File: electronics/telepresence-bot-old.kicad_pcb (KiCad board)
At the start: 4 copper layers, 100 x 100 mm, 191 parts, among them J1 STATUS, J10 Conn_01x02_Pin, J12 GND, J13 Conn_01x08_Pin, J14 IOLV / VIO, J15 Conn_02x06_Counter_Clockwise, J16 MOT_CON, J17 Conn_02x06_Counter_Clockwise, J18 MOT_CON, J19 Conn_02x06_Counter_Clockwise, J2 EXT_PWR_BTN, J20 MOT_CON, J3 IOLV_IN, J4 BATT, J5 BATT_OUT, J6 Conn_02x06_Counter_Clockwise, J7 MOT_CON, J8 VMOT, J9 BP_MOTOR_ENABLE, Q1 Q_PMOS_GDS, Q2 PMOS_GDS, Q3 2N3904, Q4 2N3904, U10 ISO7762DBQ, U11 LM1117DT-3.3, U12 SFH617A-1, U13 BTT TMC5160 Pro, U14 BTT TMC5160 Pro, U15 BTT TMC5160 Pro, U2 LM1117DT-5.0, U3 LM1117DT-3.3, U4 SFH617A-1, U5 DBG_HDR, U6 INA228, U7 BTT TMC5160 Pro, U8 SFH617A-1, U9 74LVC125

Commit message: saving before i nuke this shit
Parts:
- moved C24 2.46 mm to (228.6, 58.0), turned to 180 degrees
- moved R64 1.88 mm to (236.0, 75.2), turned to 0 degrees
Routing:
- net /3v3_compute: track 148.0 -> 33.5 mm, vias 3 -> 0
- net /SDA: track 104.5 -> 5.15 mm, vias 3 -> 1
- net GND: track 457.1 -> 362.3 mm
- net /SCL: track 66.6 -> 5.13 mm
- net Net-(D9-K): track 27.4 -> 4.52 mm
- net Net-(J1-Pin_1): track 17.7 -> 0.00 mm
- net /drivers/DRV_VIO_ISO: track 107.8 -> 95.5 mm
- net /5v_compute: track 31.1 -> 19.2 mm
- net Net-(Q3-B): track 6.47 -> 0.00 mm
- net Net-(Q4-B): track 5.15 -> 0.00 mm
- net Net-(J1-Pin_7): track 5.14 -> 0.00 mm
- net Net-(D10-K): track 3.26 -> 0.00 mm
- net Net-(D2-A): track 3.18 -> 0.00 mm
- net Net-(D11-K): track 2.94 -> 0.00 mm
- net Net-(D3-A): track 2.91 -> 0.00 mm

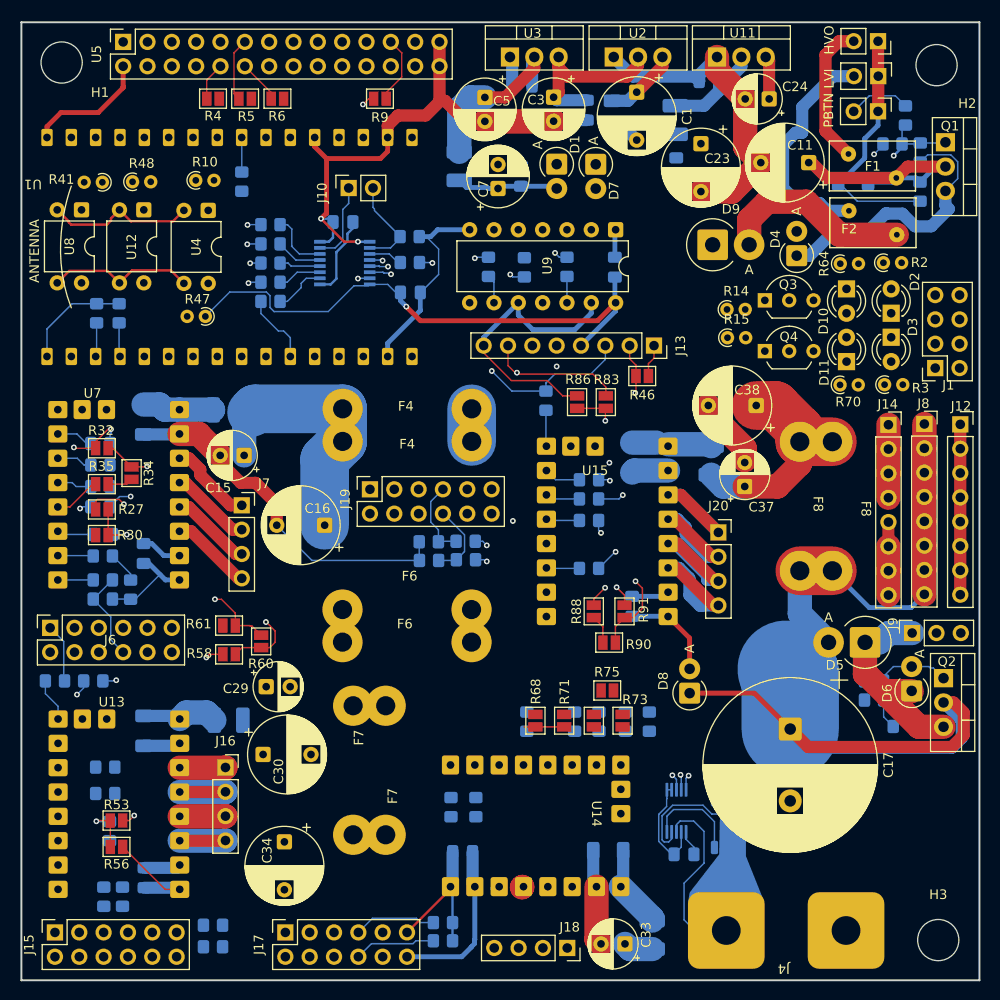
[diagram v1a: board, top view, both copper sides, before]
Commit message: Switching to a bigger PCB since cost seems negligible
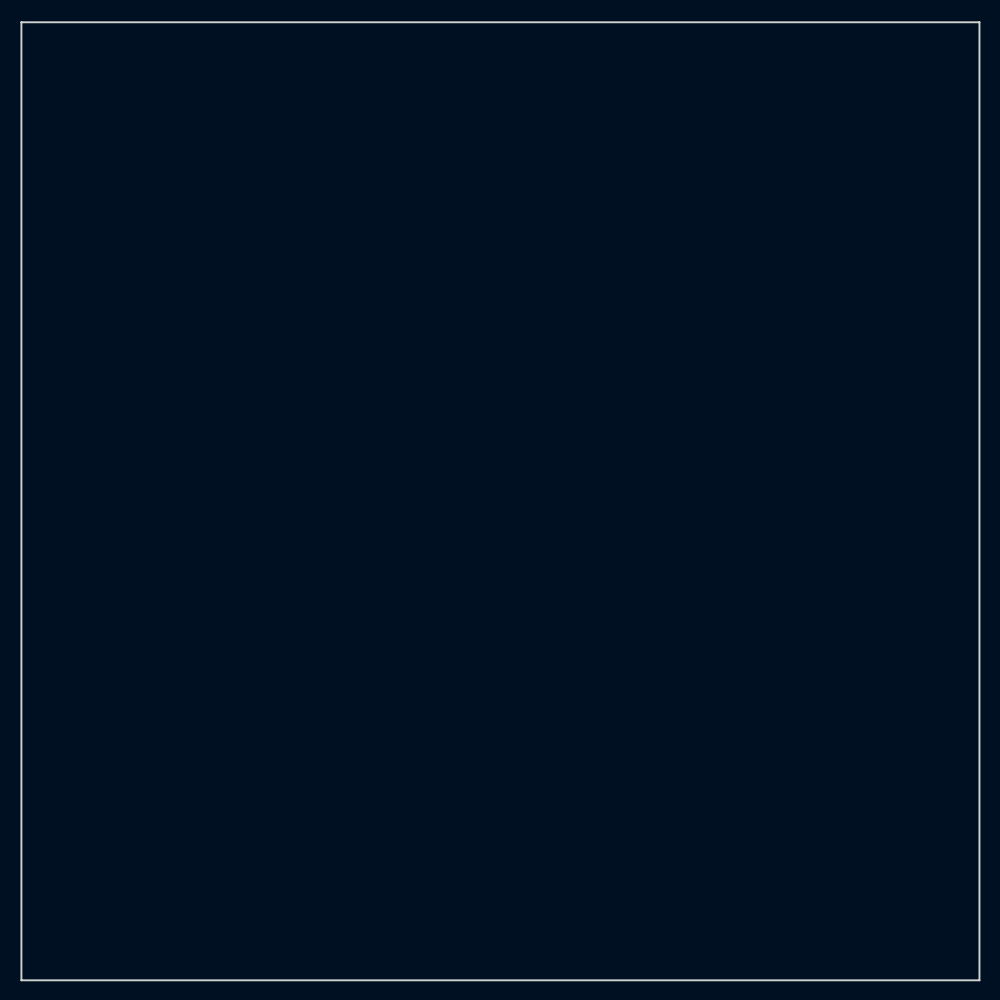
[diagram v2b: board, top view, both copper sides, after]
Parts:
- removed C1, C11, C16, C23, C30, C34, C38: 100uF, Capacitor_THT:CP_Radial_D8.0mm_P5.00mm
- removed C12, C14, C2, C28, C32, C36: 100nF, Capacitor_SMD:C_1206_3216Metric_Pad1.33x1.80mm_HandSolder
- removed C13, C20, C21, C22, C25, C26, C27, C31, C35, C4, C6, C8, C9: 100nF, Capacitor_SMD:C_0805_2012Metric_Pad1.18x1.45mm_HandSolder
- removed C15, C29, C33, C37: 4.7uF, Capacitor_THT:CP_Radial_D5.0mm_P2.50mm
- removed C17: 1000uF, Capacitor_THT:CP_Radial_D18.0mm_P7.50mm
- removed C24: 10uF, Capacitor_THT:CP_Radial_D5.0mm_P2.50mm
- removed C3, C5, C7: 100uF, Capacitor_THT:CP_Radial_D6.3mm_P2.50mm
- removed D1, D7: 3.6v, Diode_THT:D_DO-41_SOD81_P2.54mm_Vertical_AnodeUp
- removed D10, D11, D2, D3: LED, LED_THT:LED_D3.0mm
- removed D4: Zen_12v, Diode_THT:D_DO-41_SOD81_P2.54mm_Vertical_AnodeUp
- removed D5, D9: D_Schottky, Diode_THT:D_DO-201AD_P3.81mm_Vertical_AnodeUp
- removed D6: Zener-12v, Diode_THT:D_DO-41_SOD81_P2.54mm_Vertical_AnodeUp
- removed D8: 60V, Diode_THT:D_DO-41_SOD81_P2.54mm_Vertical_AnodeUp
- removed F1, F2: Polyfuse, Varistor:RV_Disc_D9mm_W5.2mm_P5mm
- removed F4, F6, F7, F8: Fuse, Fuse:XFCN XF-508P-A-B
- removed FB1, FB2: FB, Inductor_SMD:L_1210_3225Metric_Pad1.42x2.65mm_HandSolder
- removed H1, H2, H3: MountingHole_Pad_MP, MountingHole:MountingHole_4.3mm_M4_ISO7380
- removed J1: STATUS, Connector_PinSocket_2.54mm:PinSocket_2x04_P2.54mm_Vertical
- removed J10: Conn_01x02_Pin, Connector_PinSocket_2.54mm:PinSocket_1x02_P2.54mm_Vertical
- removed J12: GND, Connector_PinSocket_2.54mm:PinSocket_1x08_P2.54mm_Vertical
- removed J13: Conn_01x08_Pin, Connector_PinSocket_2.54mm:PinSocket_1x08_P2.54mm_Vertical
- removed J14: IOLV / VIO, Connector_PinSocket_2.54mm:PinSocket_1x08_P2.54mm_Vertical
- removed J15, J17, J19, J6: Conn_02x06_Counter_Clockwise, Connector_PinSocket_2.54mm:PinSocket_2x06_P2.54mm_Vertical
- removed J16, J18, J20, J7: MOT_CON, Connector_PinSocket_2.54mm:PinSocket_1x04_P2.54mm_Vertical
- removed J2: EXT_PWR_BTN, Connector_PinHeader_2.54mm:PinHeader_1x02_P2.54mm_Vertical
- removed J3: IOLV_IN, Connector_PinHeader_2.54mm:PinHeader_1x02_P2.54mm_Vertical
- removed J4: BATT, Connector:BATT_CONNECTOR
- removed J5: BATT_OUT, Connector_PinSocket_2.54mm:PinSocket_1x02_P2.54mm_Vertical
- removed J8: VMOT, Connector_PinSocket_2.54mm:PinSocket_1x08_P2.54mm_Vertical
- removed J9: BP_MOTOR_ENABLE, Connector_PinSocket_2.54mm:PinSocket_1x03_P2.54mm_Vertical
- removed L1, L3, L4, L5: ferrite, Inductor_SMD:L_1210_3225Metric_Pad1.42x2.65mm_HandSolder
- removed Q1: Q_PMOS_GDS, Package_TO_SOT_THT:TO-220-3_Vertical
- removed Q2: PMOS_GDS, Package_TO_SOT_THT:TO-220-3_Vertical
- removed Q3, Q4: 2N3904, Package_TO_SOT_THT:TO-92_Inline_Wide
- removed R1, R18, R19, R20, R21, R23, R24, R25, R26, R28, R29, R31, R33, R42, R43, R44, R45, R49, R50, R51, R52, R54, R55, R57, R59, R65, R66, R67, R69, R7, R72, R74, R80, R81, R82, R84, R87, R89: 33R, Resistor_SMD:R_0805_2012Metric_Pad1.20x1.40mm_HandSolder
- removed R10, R3, R41, R48: 220R, Resistor_THT:R_Axial_DIN0204_L3.6mm_D1.6mm_P1.90mm_Vertical
- removed R11, R13, R16, R17, R39, R40: 10k, Resistor_SMD:R_0805_2012Metric_Pad1.20x1.40mm_HandSolder
- removed R12, R36, R37, R38, R62, R63, R77, R78, R8, R92, R93, R94: 100k, Resistor_SMD:R_0805_2012Metric_Pad1.20x1.40mm_HandSolder
- removed R14, R15, R47: 1k, Resistor_THT:R_Axial_DIN0204_L3.6mm_D1.6mm_P1.90mm_Vertical
- removed R2, R64, R70: 470R, Resistor_THT:R_Axial_DIN0204_L3.6mm_D1.6mm_P1.90mm_Vertical
- removed R22: 1.5m, Resistor_SMD:R_Shunt_Vishay_WSK2512_6332Metric_T2.66mm
- removed R27, R30, R32, R34, R35, R4, R46, R5, R53, R56, R58, R6, R60, R61, R68, R71, R73, R75, R76, R83, R86, R88, R9, R90, R91: 0, Jumper:SolderJumper-2_P1.3mm_Open_Pad1.0x1.5mm
- removed U1: ~, RF_Module:ESP32-C5-DevKitC-1-v1.2
- removed U10: ISO7762DBQ, Package_SO:SSOP-16_3.9x4.9mm_P0.635mm
- removed U11, U3: LM1117DT-3.3, Package_TO_SOT_THT:TO-220-3_Vertical
- removed U12, U4, U8: SFH617A-1, Package_DIP:DIP-4_W7.62mm
- removed U13, U14, U15, U7: BTT TMC5160 Pro, Module:BTT-TMC5160PRO-v1.0
- removed U2: LM1117DT-5.0, Package_TO_SOT_THT:TO-220-3_Vertical
- removed U5: DBG_HDR, Connector_PinSocket_2.54mm:PinSocket_2x14_P2.54mm_Vertical
- removed U6: INA228, Package_SO:VSSOP-10_3x3mm_P0.5mm
- removed U9: 74LVC125, Package_DIP:DIP-14_W7.62mm
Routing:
- net GND: track 362.3 -> 0.00 mm, vias 2 -> 0
- net VMOT: track 135.7 -> 0.00 mm
- net /drivers/DRV_CLK_ISO: track 134.1 -> 0.00 mm, vias 3 -> 0
- net /drivers/DRV_ENABLE_ISO: track 101.8 -> 0.00 mm, vias 2 -> 0
- net /drivers/DRV_VIO_ISO: track 95.5 -> 0.00 mm, vias 1 -> 0
- net /drivers/DRV_MOSI_ISO: track 59.3 -> 0.00 mm, vias 2 -> 0
- net /drivers/DRV_CS_ISO: track 57.1 -> 0.00 mm, vias 3 -> 0
- net /MOTOR_POWER_RAIL: track 50.9 -> 0.00 mm
- net /drivers/DRV_SCK_ISO: track 49.9 -> 0.00 mm, vias 2 -> 0
- net /drivers/motor_driver3/_CLK_DCO: track 47.3 -> 0.00 mm, vias 2 -> 0
- net /drivers/motor_driver3/_MOSI: track 41.0 -> 0.00 mm, vias 2 -> 0
- net /IOLV_IN: track 35.6 -> 0.00 mm
- net /3v3_compute: track 33.5 -> 0.00 mm
- net /drivers/DRV_MOSI_LAST: track 33.3 -> 0.00 mm, vias 2 -> 0
- net /drivers/motor_driver1/_MOSI: track 31.8 -> 0.00 mm, vias 2 -> 0
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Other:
- board text removed: "HVO"
- board text removed: "LVI"
- board text removed: "PBTN"
